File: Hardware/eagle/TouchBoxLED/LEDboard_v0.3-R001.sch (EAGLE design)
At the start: 11 parts, among them X2 22-23-2021

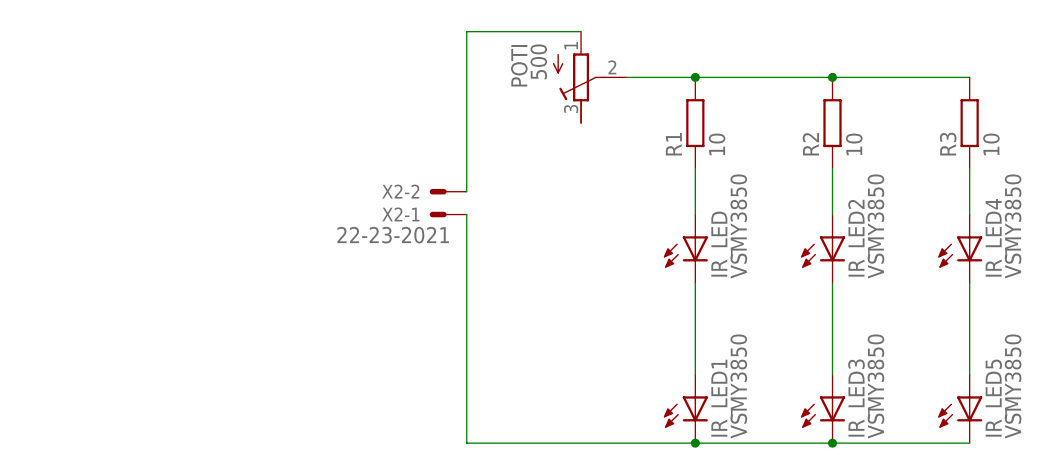
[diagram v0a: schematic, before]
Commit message: new PressureBase design restructuring of design folder
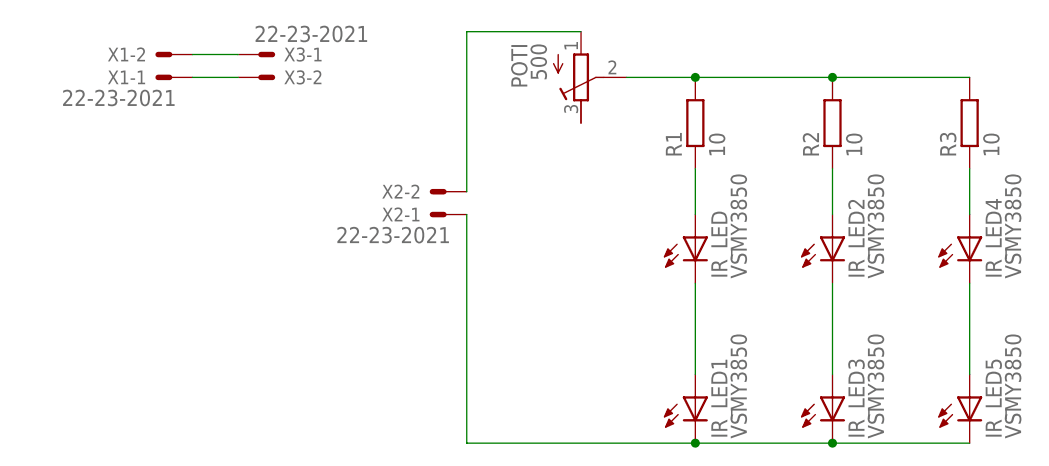
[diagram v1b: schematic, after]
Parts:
- added X1, X3: 22-23-2021, con-molex:22-23-2021
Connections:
- new net N$10: X1-2.S, X3-1.S
- new net N$11: X1-1.S, X3-2.S
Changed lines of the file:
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@@
 <?xml version="1.0" encoding="utf-8"?>
 <!DOCTYPE eagle SYSTEM "eagle.dtd">
-<eagle version="6.5.0">
+<eagle version="9.5.1">
 <drawing>
 <settings>
 <setting alwaysvectorfont="no"/>
+<setting keepoldvectorfont="yes"/>
 <setting verticaltext="up"/>
 </settings>
@@
 <part name="POTI" library="rcl" deviceset="R-TRIMM" device="64Y" value="500"/>
 <part name="X2" library="con-molex" deviceset="22-23-2021" device=""/>
+<part name="X1" library="con-molex" deviceset="22-23-2021" device=""/>
+<part name="X3" library="con-molex" deviceset="22-23-2021" device=""/>
 </parts>
 <sheets>
@@
 </plain>
 <instances>
-<instance part="IR_LED" gate="G$1" x="5.08" y="78.74"/>
-<instance part="IR_LED1" gate="G$1" x="5.08" y="60.96"/>
-<instance part="R1" gate="G$1" x="5.08" y="91.44" rot="R90"/>
-<instance part="IR_LED2" gate="G$1" x="20.32" y="78.74"/>
-<instance part="IR_LED3" gate="G$1" x="20.32" y="60.96"/>
-<instance part="R2" gate="G$1" x="20.32" y="91.44" rot="R90"/>
-<instance part="IR_LED4" gate="G$1" x="35.56" y="78.74"/>
-<instance part="IR_LED5" gate="G$1" x="35.56" y="60.96"/>
-<instance part="R3" gate="G$1" x="35.56" y="91.44" rot="R90"/>
-<instance part="POTI" gate="G$1" x="-7.62" y="96.52" rot="MR180"/>
-<instance part="X2" gate="-1" x="-22.86" y="81.28" rot="R180"/>
-<instance part="X2" gate="-2" x="-22.86" y="83.82" rot="R180"/>
+<instance part="IR_LED" gate="G$1" x="5.08" y="78.74" smashed="yes">
+<attribute name="NAME" x="8.636" y="74.168" size="1.778" layer="95" rot="R90"/>
+<attribute name="VALUE" x="10.795" y="74.168" size="1.778" layer="96" rot="R90"/>
+</instance>
+<instance part="IR_LED1" gate="G$1" x="5.08" y="60.96" smashed="yes">
+<attribute name="NAME" x="8.636" y="56.388" size="1.778" layer="95" rot="R90"/>
+<attribute name="VALUE" x="10.795" y="56.388" size="1.778" layer="96" rot="R90"/>
+</instance>
+<instance part="R1" gate="G$1" x="5.08" y="91.44" smashed="yes" rot="R90">
+<attribute name="NAME" x="3.5814" y="87.63" size="1.778" layer="95" rot="R90"/>
+<attribute name="VALUE" x="8.382" y="87.63" size="1.778" layer="96" rot="R90"/>
+</instance>
+<instance part="IR_LED2" gate="G$1" x="20.32" y="78.74" smashed="yes">
+<attribute name="NAME" x="23.876" y="74.168" size="1.778" layer="95" rot="R90"/>
+<attribute name="VALUE" x="26.035" y="74.168" size="1.778" layer="96" rot="R90"/>
+</instance>
+<instance part="IR_LED3" gate="G$1" x="20.32" y="60.96" smashed="yes">
+<attribute name="NAME" x="23.876" y="56.388" size="1.778" layer="95" rot="R90"/>
+<attribute name="VALUE" x="26.035" y="56.388" size="1.778" layer="96" rot="R90"/>
+</instance>
+<instance part="R2" gate="G$1" x="20.32" y="91.44" smashed="yes" rot="R90">
+<attribute name="NAME" x="18.8214" y="87.63" size="1.778" layer="95" rot="R90"/>
+<attribute name="VALUE" x="23.622" y="87.63" size="1.778" layer="96" rot="R90"/>
+</instance>
+<instance part="IR_LED4" gate="G$1" x="35.56" y="78.74" smashed="yes">
+<attribute name="NAME" x="39.116" y="74.168" size="1.778" layer="95" rot="R90"/>
+<attribute name="VALUE" x="41.275" y="74.168" size="1.778" layer="96" rot="R90"/>
+</instance>
+<instance part="IR_LED5" gate="G$1" x="35.56" y="60.96" smashed="yes">
+<attribute name="NAME" x="39.116" y="56.388" size="1.778" layer="95" rot="R90"/>
+<attribute name="VALUE" x="41.275" y="56.388" size="1.778" layer="96" rot="R90"/>
+</instance>
+<instance part="R3" gate="G$1" x="35.56" y="91.44" smashed="yes" rot="R90">
+<attribute name="NAME" x="34.0614" y="87.63" size="1.778" layer="95" rot="R90"/>
+<attribute name="VALUE" x="38.862" y="87.63" size="1.778" layer="96" rot="R90"/>
+</instance>
+<instance part="POTI" gate="G$1" x="-7.62" y="96.52" smashed="yes" rot="MR180">
+<attribute name="NAME" x="-13.589" y="100.33" size="1.778" layer="95" rot="MR270"/>
+<attribute name="VALUE" x="-11.43" y="100.33" size="1.778" layer="96" rot="MR270"/>
+</instance>
+<instance part="X2" gate="-1" x="-22.86" y="81.28" smashed="yes" rot="R180">
+<attribute name="NAME" x="-25.4" y="82.042" size="1.524" layer="95" rot="R180"/>
+<attribute name="VALUE" x="-22.098" y="79.883" size="1.778" layer="96" rot="R180"/>
+</instance>
+<instance part="X2" gate="-2" x="-22.86" y="83.82" smashed="yes" rot="R180">
+<attribute name="NAME" x="-25.4" y="84.582" size="1.524" layer="95" rot="R180"/>
+</instance>
+<instance part="X1" gate="-1" x="-53.34" y="96.52" smashed="yes" rot="R180">
+<attribute name="NAME" x="-55.88" y="97.282" size="1.524" layer="95" rot="R180"/>
+<attribute name="VALUE" x="-52.578" y="95.123" size="1.778" layer="96" rot="R180"/>
+</instance>
+<instance part="X1" gate="-2" x="-53.34" y="99.06" smashed="yes" rot="R180">
+<attribute name="NAME" x="-55.88" y="99.822" size="1.524" layer="95" rot="R180"/>
+</instance>
+<instance part="X3" gate="-1" x="-43.18" y="99.06" smashed="yes">
+<attribute name="NAME" x="-40.64" y="98.298" size="1.524" layer="95"/>
+<attribute name="VALUE" x="-43.942" y="100.457" size="1.778" layer="96"/>
+</instance>
+<instance part="X3" gate="-2" x="-43.18" y="96.52" smashed="yes">
+<attribute name="NAME" x="-40.64" y="95.758" size="1.524" layer="95"/>
+</instance>
 </instances>
 <busses>
@@
 </segment>
 </net>
+<net name="N$10" class="0">
+<segment>
+<pinref part="X1" gate="-2" pin="S"/>
+<pinref part="X3" gate="-1" pin="S"/>
+<wire x1="-50.8" y1="99.06" x2="-45.72" y2="99.06" width="0.1524" layer="91"/>
+</segment>
+</net>
+<net name="N$11" class="0">
+<segment>
+<pinref part="X1" gate="-1" pin="S"/>
+<pinref part="X3" gate="-2" pin="S"/>
+<wire x1="-50.8" y1="96.52" x2="-45.72" y2="96.52" width="0.1524" layer="91"/>
+</segment>
+</net>
